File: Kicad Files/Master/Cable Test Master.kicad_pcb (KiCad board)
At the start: 2 copper layers, 50.8 x 62.2 mm, 64 parts, among them J1 RJ45, J2 RJ12, J3 PWR, J4 ISP, Q1 BSS84, Q10 2N7002, Q11 2N7002, Q12 2N7002, Q13 2N7002, Q14 2N7002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

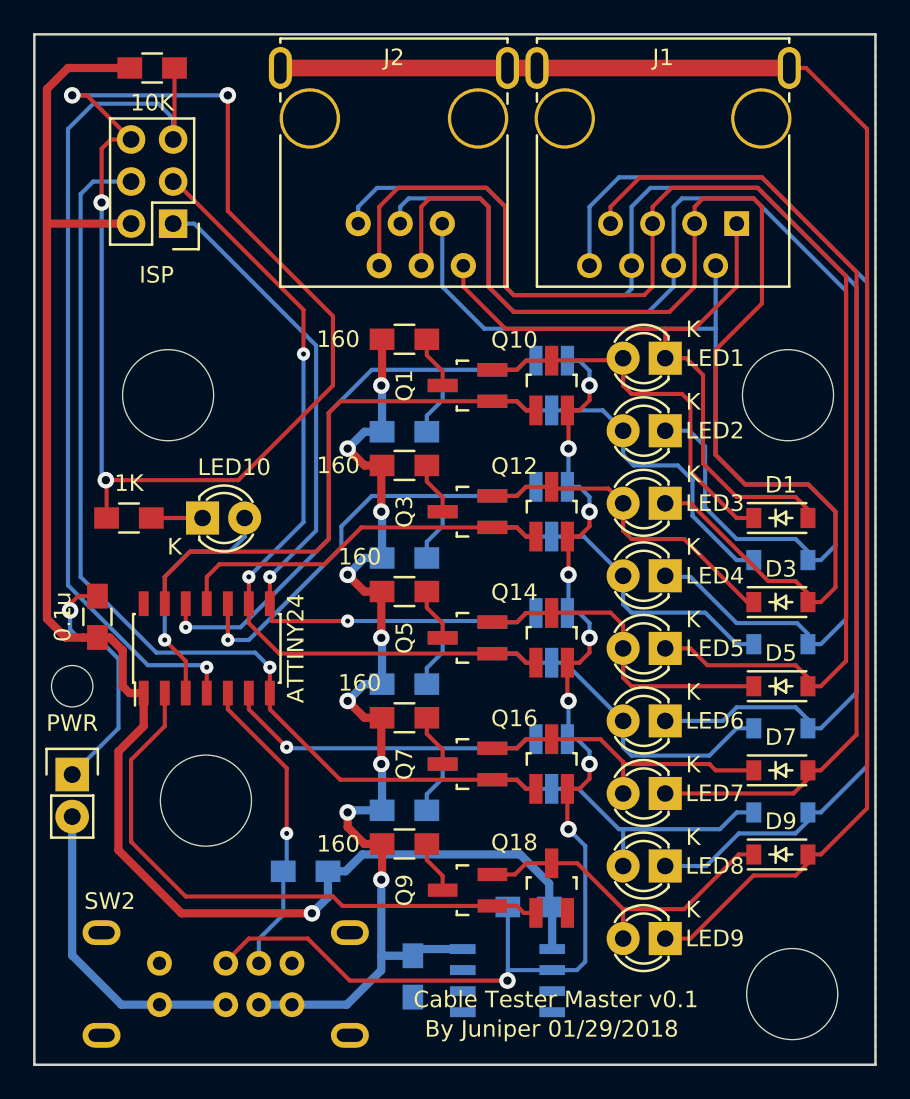
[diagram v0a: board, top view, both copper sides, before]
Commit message: Fix mounting holes and RJ12 footprint
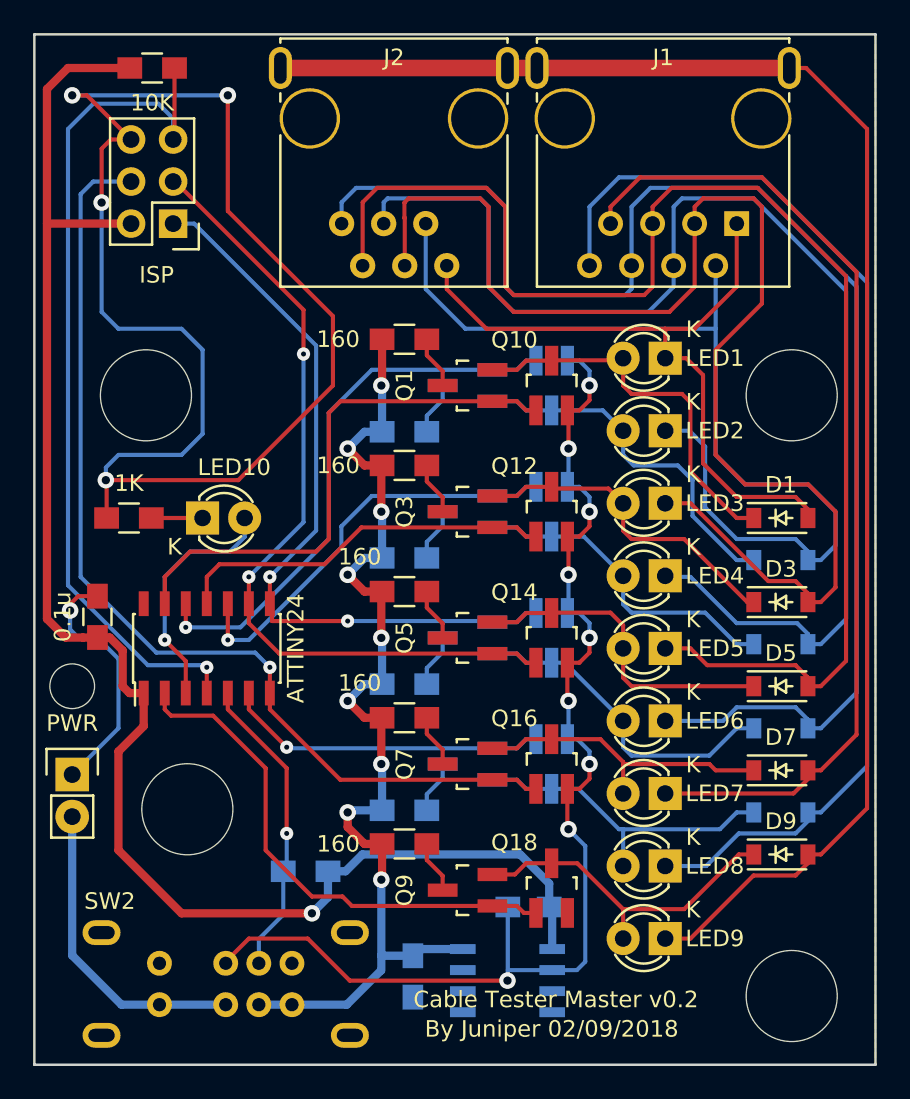
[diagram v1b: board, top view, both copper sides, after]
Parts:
- REF**: footprint Mounting_Holes:MountingHole_2-5mm -> Mounting_Holes:MountingHole_2-7mm
- moved REF** 1.34 mm to (118.5, 85.3)
- moved REF** 1.24 mm to (121.0, 110.3)
- moved REF** 0.22 mm to (157.5, 85.3)
- moved REF** 0.12 mm to (157.5, 121.6)
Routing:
- net GND: track 163.1 -> 172.4 mm
- net /MOSFET Drive/B0: track 36.1 -> 31.5 mm
- net /3: track 78.7 -> 79.9 mm
- net /4: track 75.2 -> 76.4 mm
- net /6: track 83.3 -> 84.5 mm
- net /5: track 81.5 -> 82.7 mm
- net /2: track 60.4 -> 61.5 mm
- net /1: track 41.5 -> 42.6 mm
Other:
- board text added: "By Juniper 02/09/2018"
- board text added: "Cable Tester Master v0.2"
- board text removed: "By Juniper 01/29/2018"
- board text removed: "Cable Tester Master v0.1"
